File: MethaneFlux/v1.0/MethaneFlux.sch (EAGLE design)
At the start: 59 parts, among them J1 282836-5, J2 282836-5, J3 282836-5, J4 282836-5, J5 GTFH08131YHR, P1 282837-2, U1 ADS1115IDGSR, U2 BME680, U3 74LVC125APW,118, U4 BME680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

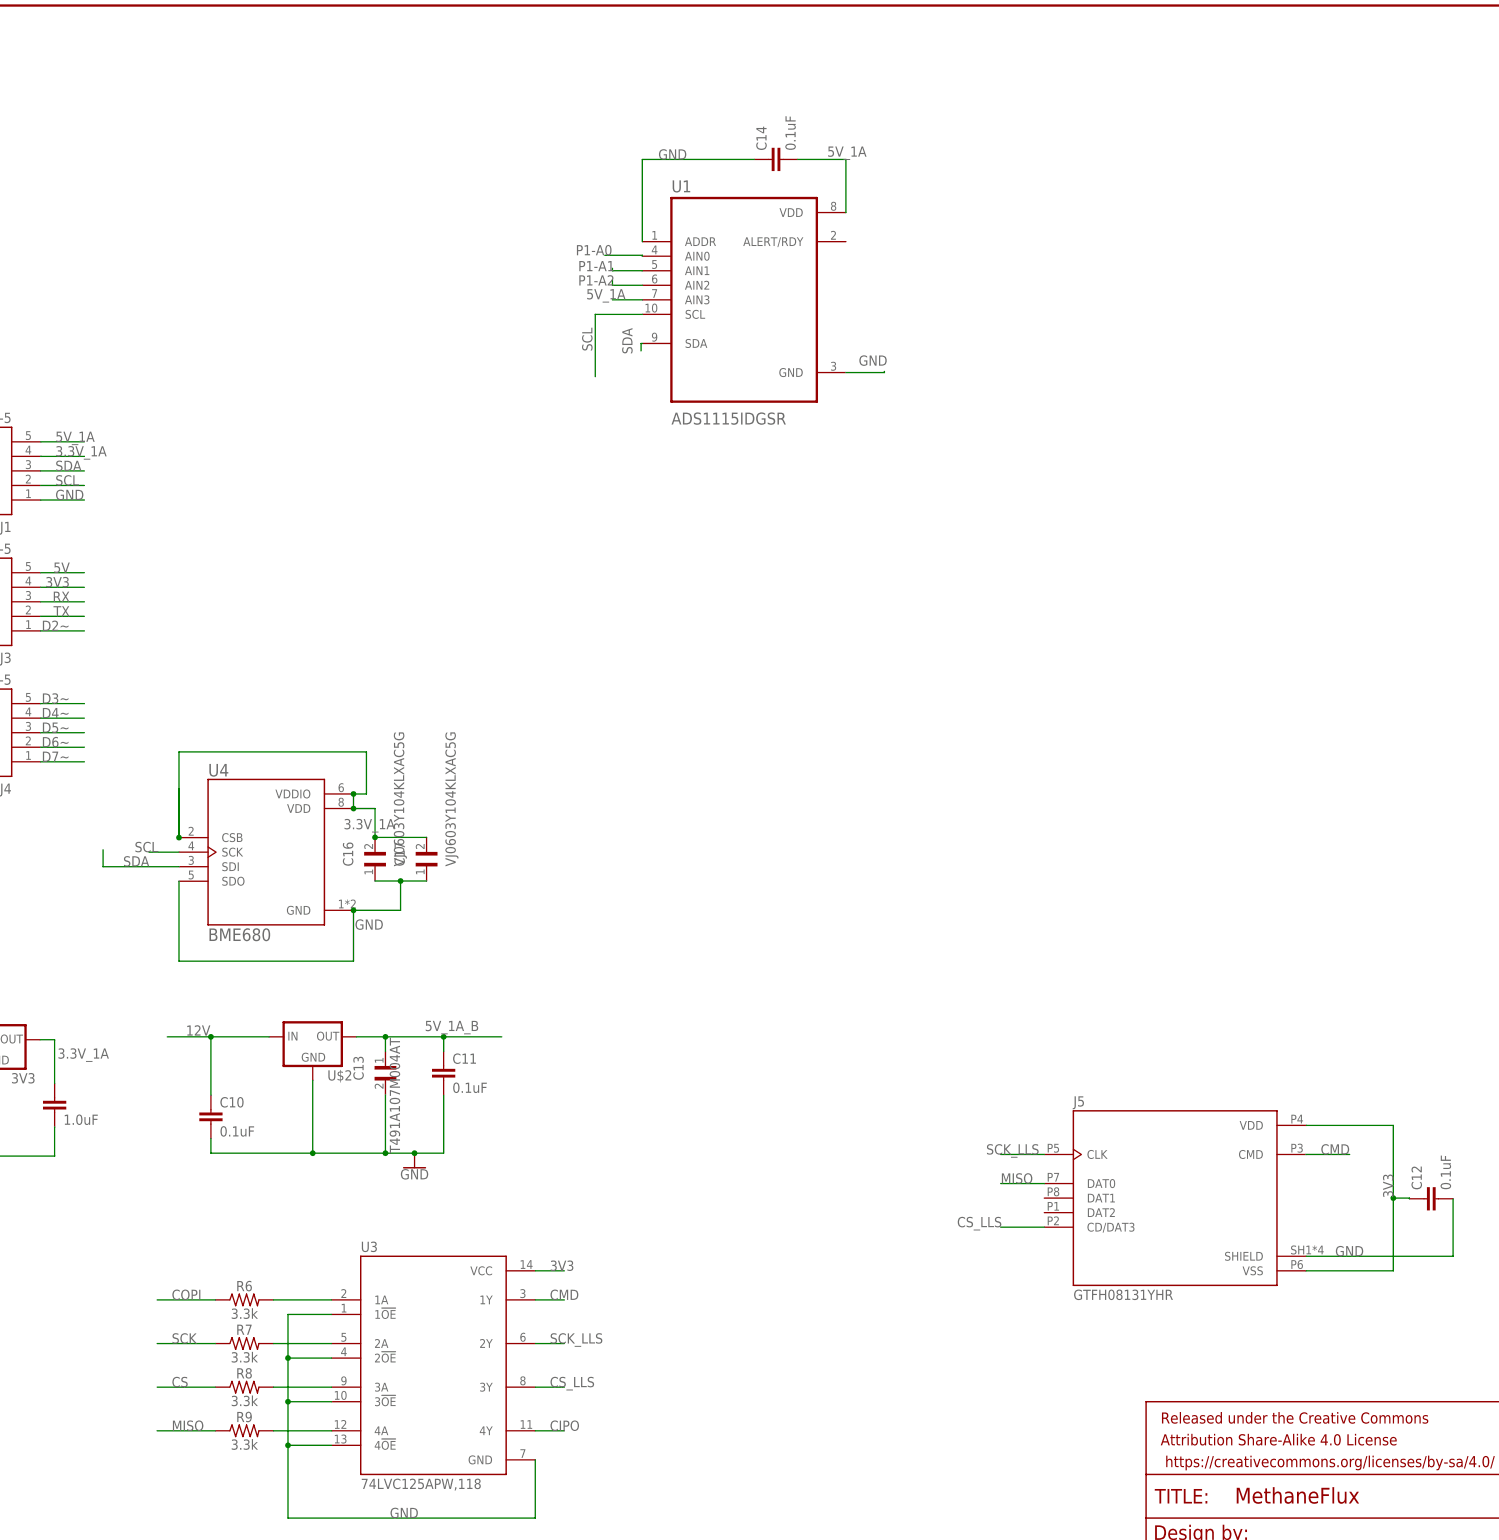
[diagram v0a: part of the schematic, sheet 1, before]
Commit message: Add files via upload
Added a level shifter for the BME680 for 5V I2C to 3V I2C. Added ferrite bead and 10k resistors to the ADC.
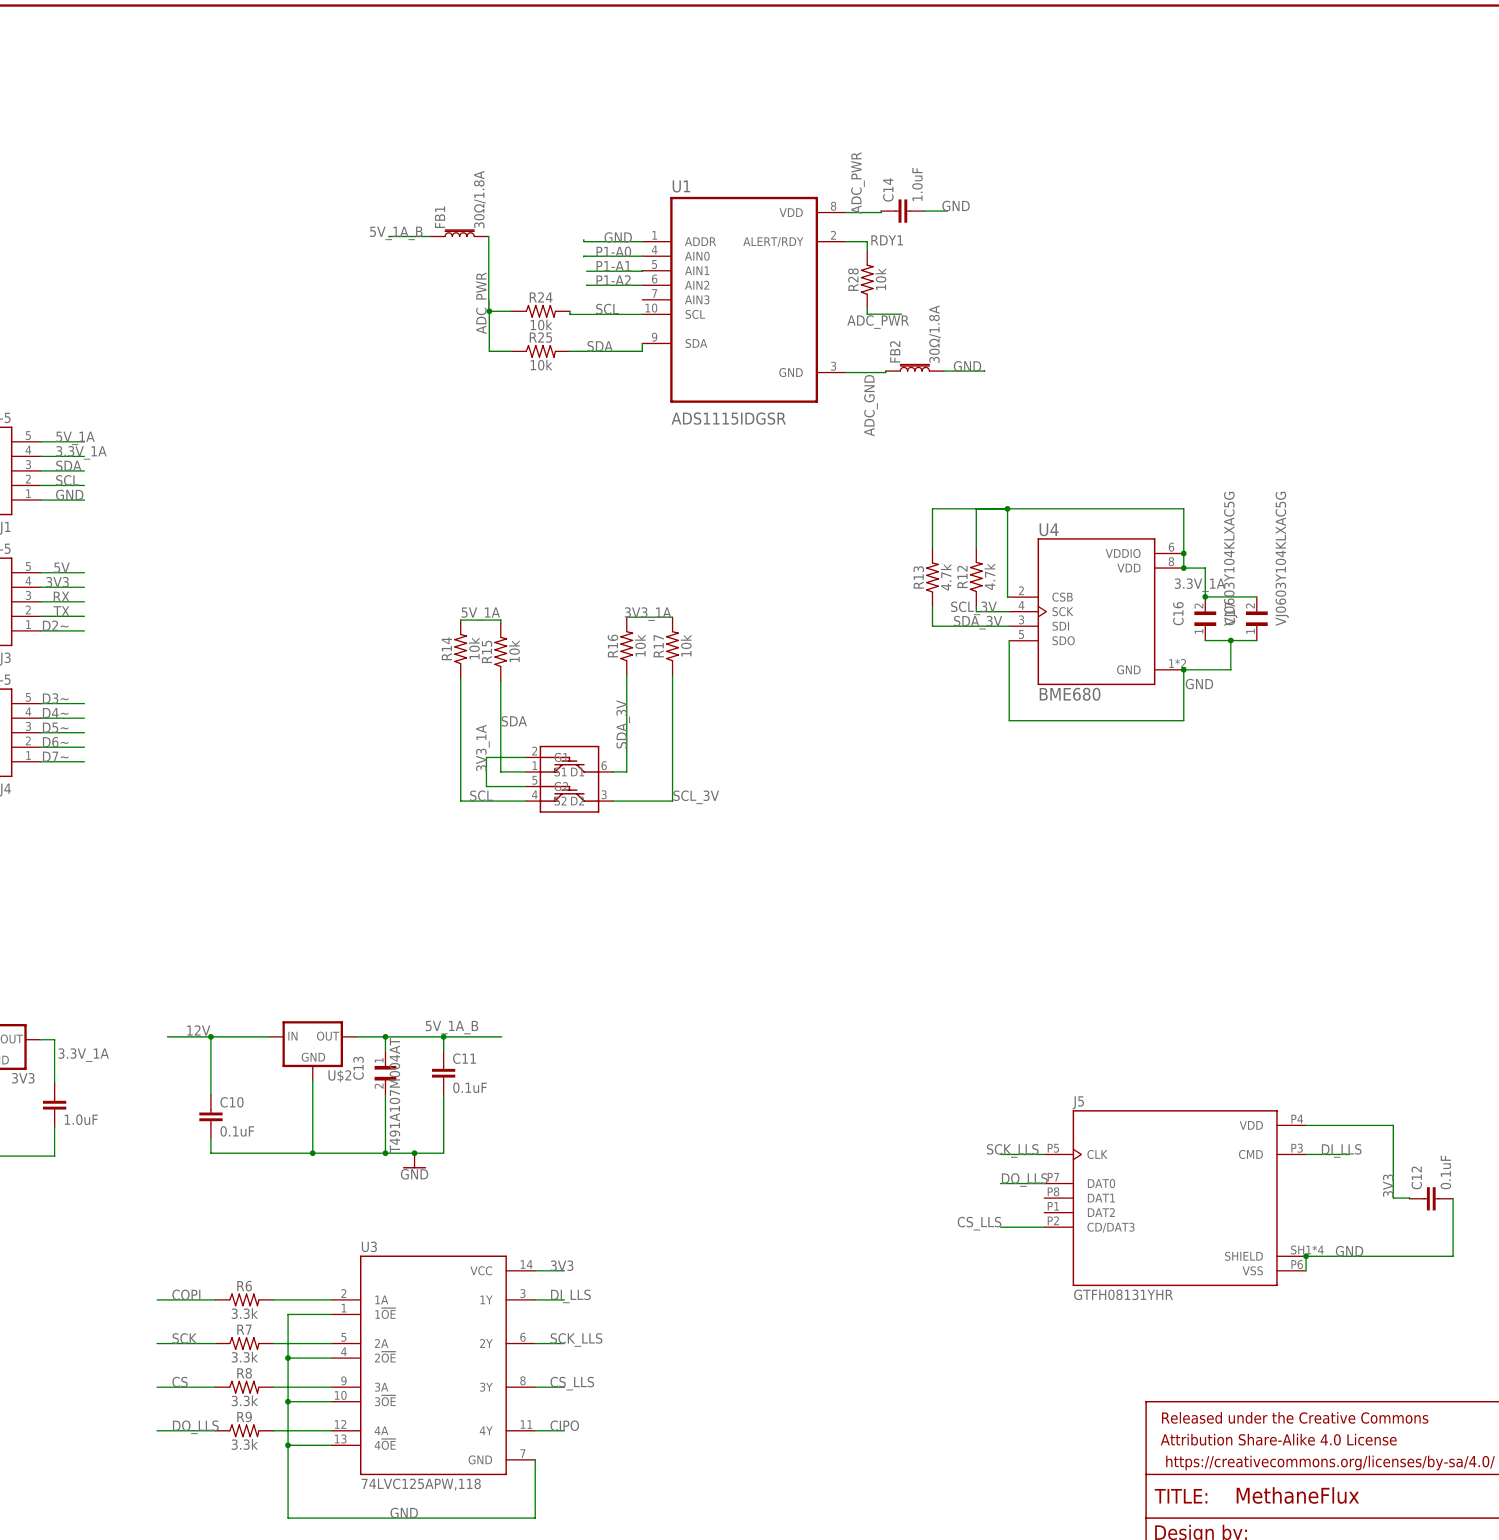
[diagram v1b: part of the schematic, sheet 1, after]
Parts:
- added FB1, FB2, FB3, FB4: 30Ω/1.8A, SparkFun-Coils:FERRITE_BEAD-0603
- added R10, R11, R12, R13: 4.7k, SparkFun-Resistors:4.7KOHM-0603-1/10W-1%
- added R14, R15, R16, R17, R20, R21, R22, R23, R24, R25, R26, R27, R28, R29: 10k, SparkFun-Resistors:10KOHM-0603-1/10W-1%
- added U$3, U$4: 2N7002DW, 2N7002DW:2N7002DW
- C14, C7: value 0.1uF -> 1.0uF; device SparkFun-Capacitors:0.1UF-0603-25V-5% -> SparkFun-Capacitors:1.0UF-0603-16V-10%
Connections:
- net CMD renamed DI_LLS
- net MISO renamed DO_LLS
- new net 3V3_1A: R16.2, R17.2, U$3.G1, U$3.G2
- new net ADC_GND: FB2.1, U1.GND
- new net ADC_PWR: C14.1, FB1.2, R24.1, R25.1, R28.1, U1.VDD
- new net P2-SDA_3V: R10.1, R22.1, U$4.D1, U2.SDI
- new net P2_ADC_GND: FB4.1, U5.GND
- new net P2_ADC_PWR: C7.2, FB3.2, R26.2, R27.2, R29.2, U5.ADDR, U5.VDD
- new net P2_SCL_3V: R11.1, R23.1, U$4.D2, U2.SCK
- new net RDY1: R28.2, U1.ALERT/RDY
- new net RDY2: R29.1, U5.ALERT/RDY
- new net SCL_3V: R12.1, R17.1, U$3.D2, U4.SCK
- new net SDA_3V: R13.1, R16.1, U$3.D1, U4.SDI
- net 3.3V_1A: now also R12.2, R13.2
- net 3V3: no longer J5.VSS
- net 5V_1A: now also R14.2, R15.2; no longer C14.2, U1.AIN3, U1.VDD
- net 5V_1A_B: now also FB1.1
- net GND: now also C14.2, FB2.2, J5.VSS; no longer C14.1, U1.GND
- net P2-A0: now also U5.AIN3; no longer U5.AIN0
- net P2_3V3: now also R10.2, R11.2, R22.2, R23.2, U$4.G1, U$4.G2
- net P2_5V: now also FB3.1, R20.2, R21.2; no longer C7.2, U5.ADDR, U5.AIN3, U5.VDD
- net P2_GND: now also FB4.2; no longer U5.GND
- net P2_SCL: now also R20.1, R26.1, U$4.S2; no longer U2.SCK
- net P2_SDA: now also R21.1, R27.1, U$4.S1; no longer U2.SDI
- net SCL: now also R14.1, R24.2, U$3.S2; no longer U4.SCK
- net SDA: now also R15.1, R25.2, U$3.S1; no longer U4.SDI
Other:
- moved on the sheet: C14, C16, C17, C7, U4
